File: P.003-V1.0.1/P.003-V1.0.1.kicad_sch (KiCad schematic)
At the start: 0 parts

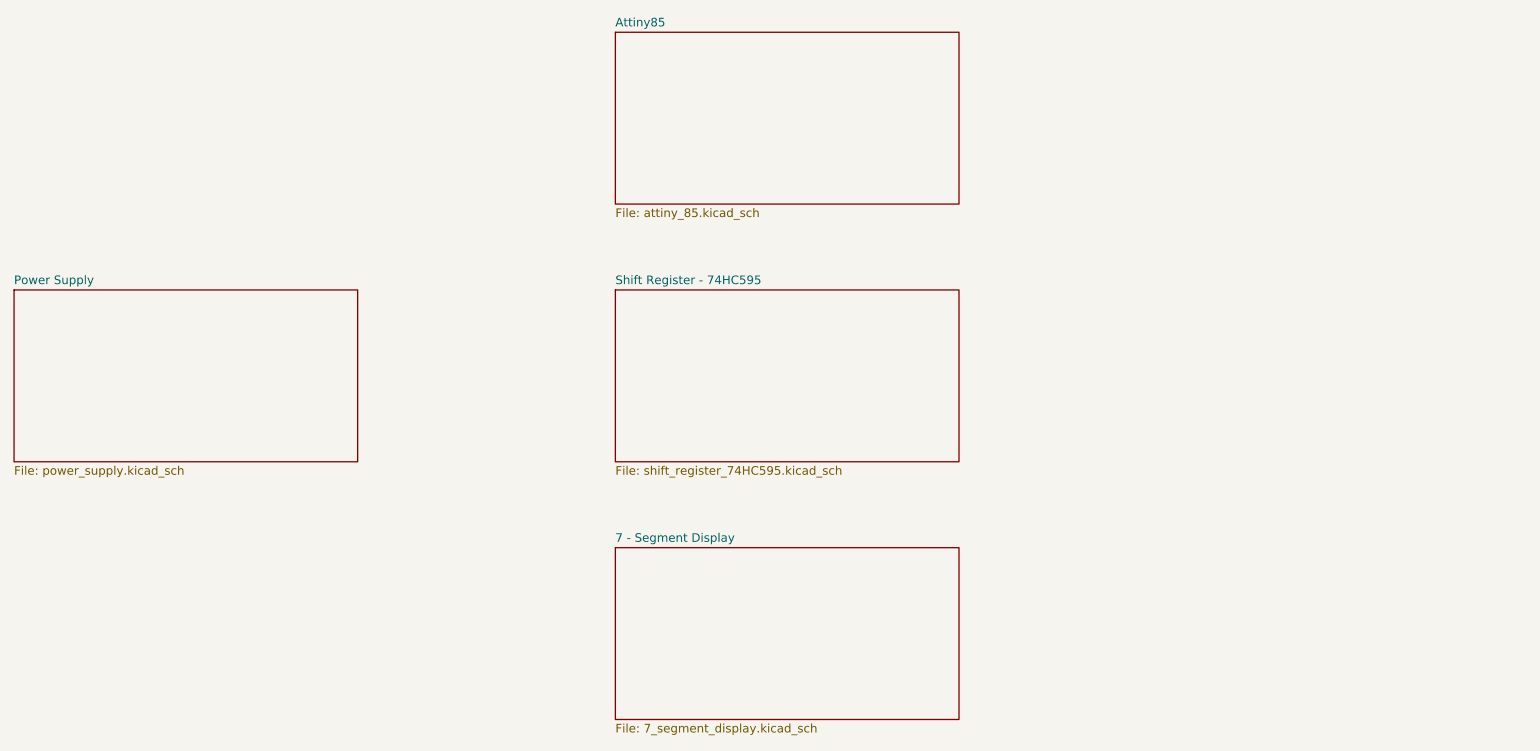
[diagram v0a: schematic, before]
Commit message: add kicad
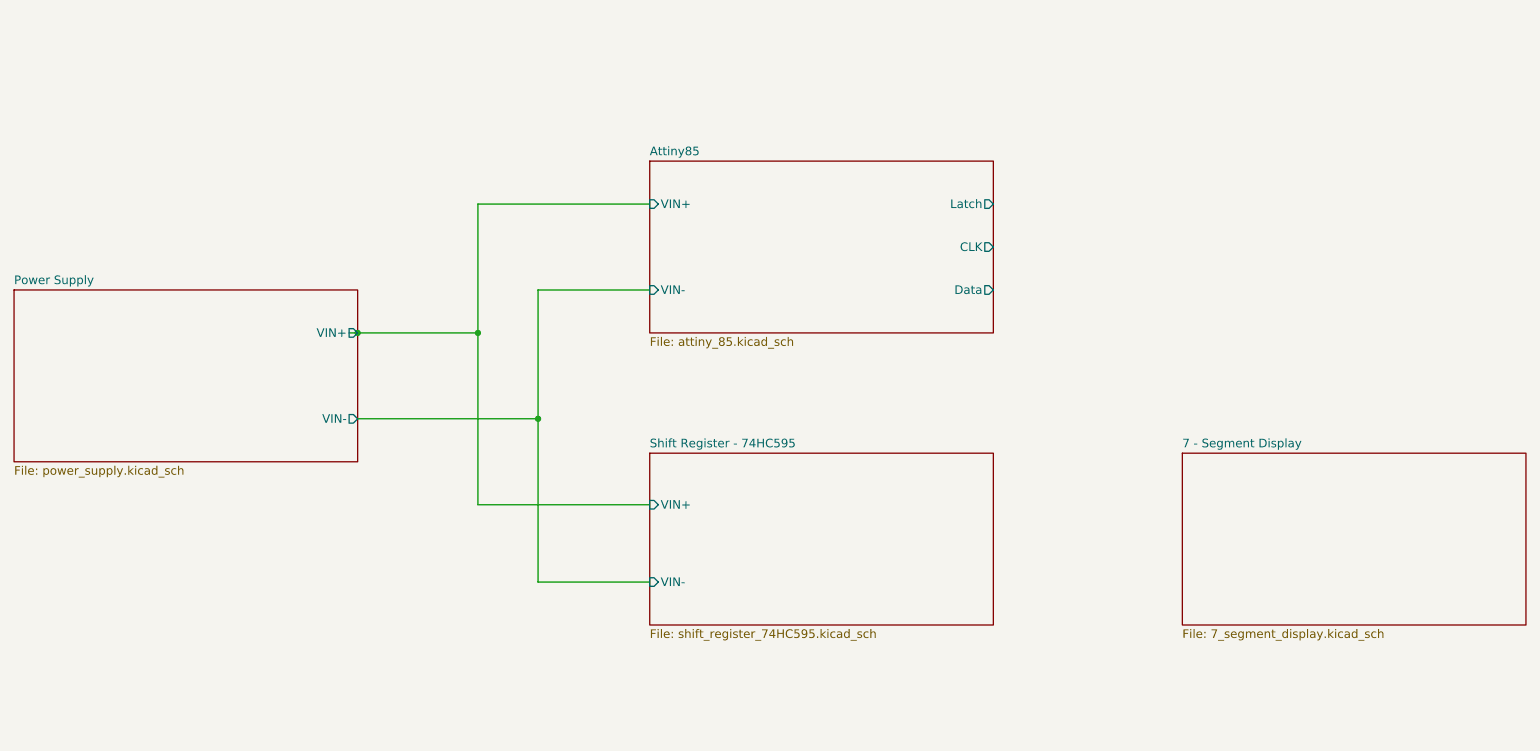
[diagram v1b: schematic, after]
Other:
- sheet Attiny85 ports: added CLK, Data, Latch, VIN+, VIN-; removed none
- sheet Power Supply ports: added VIN+, VIN-; removed none
- sheet Shift Register - 74HC595 ports: added VIN+, VIN-; removed none
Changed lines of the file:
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@@
 	(generator_version "10.0")
 	(paper "A4")
+	(junction
+		(at 88.9 69.85)
+		(diameter 0)
+		(color 0 0 0 0)
+	)
+	(junction
+		(at 106.68 69.85)
+		(diameter 0)
+		(color 0 0 0 0)
+	)
+	(junction
+		(at 115.57 82.55)
+		(diameter 0)
+		(color 0 0 0 0)
+	)
+	(wire
+		(pts
+			(xy 115.57 63.5) (xy 115.57 82.55)
+		)
+		(stroke
+			(width 0)
+			(type default)
+		)
+	)
+	(wire
+		(pts
+			(xy 106.68 95.25) (xy 132.08 95.25)
+		)
+		(stroke
+			(width 0)
+			(type default)
+		)
+	)
+	(wire
+		(pts
+			(xy 88.9 82.55) (xy 115.57 82.55)
+		)
+		(stroke
+			(width 0)
+			(type default)
+		)
+	)
+	(wire
+		(pts
+			(xy 106.68 50.8) (xy 132.08 50.8)
+		)
+		(stroke
+			(width 0)
+			(type default)
+		)
+	)
+	(wire
+		(pts
+			(xy 106.68 69.85) (xy 106.68 95.25)
+		)
+		(stroke
+			(width 0)
+			(type default)
+		)
+	)
+	(wire
+		(pts
+			(xy 115.57 106.68) (xy 115.57 82.55)
+		)
+		(stroke
+			(width 0)
+			(type default)
+		)
+	)
+	(wire
+		(pts
+			(xy 115.57 63.5) (xy 132.08 63.5)
+		)
+		(stroke
+			(width 0)
+			(type default)
+		)
+	)
+	(wire
+		(pts
+			(xy 87.63 69.85) (xy 88.9 69.85)
+		)
+		(stroke
+			(width 0)
+			(type default)
+		)
+	)
+	(wire
+		(pts
+			(xy 132.08 106.68) (xy 115.57 106.68)
+		)
+		(stroke
+			(width 0)
+			(type default)
+		)
+	)
+	(wire
+		(pts
+			(xy 106.68 50.8) (xy 106.68 69.85)
+		)
+		(stroke
+			(width 0)
+			(type default)
+		)
+	)
+	(wire
+		(pts
+			(xy 88.9 69.85) (xy 106.68 69.85)
+		)
+		(stroke
+			(width 0)
+			(type default)
+		)
+	)
 	(sheet
-		(at 127 63.5)
+		(at 132.08 87.63)
 		(size 50.8 25.4)
 		(exclude_from_sim no)
@@
 		)
 		(property "Sheetname" "Shift Register - 74HC595"
-			(at 127 62.7884 0)
+			(at 132.08 86.9184 0)
 			(show_name yes)
 			(do_not_autoplace no)
@@
 		)
 		(property "Sheetfile" "shift_register_74HC595.kicad_sch"
-			(at 127 89.4846 0)
+			(at 132.08 113.6146 0)
 			(show_name yes)
 			(do_not_autoplace no)
@@
 				)
 				(justify left top)
+			)
+		)
+		(pin "VIN+" input
+			(at 132.08 95.25 180)
+			(effects
+				(font
+					(size 1.27 1.27)
+				)
+				(justify left)
+			)
+		)
+		(pin "VIN-" input
+			(at 132.08 106.68 180)
+			(effects
+				(font
+					(size 1.27 1.27)
+				)
+				(justify left)
 			)
 		)
@@
 	)
 	(sheet
-		(at 127 101.6)
+		(at 210.82 87.63)
 		(size 50.8 25.4)
 		(exclude_from_sim no)
@@
 		)
 		(property "Sheetname" "7 - Segment Display"
-			(at 127 100.8884 0)
+			(at 210.82 86.9184 0)
 			(show_name yes)
 			(do_not_autoplace no)
@@
 		)
 		(property "Sheetfile" "7_segment_display.kicad_sch"
-			(at 127 127.5846 0)
+			(at 210.82 113.6146 0)
 			(show_name yes)
 			(do_not_autoplace no)
@@
 			)
 		)
+		(pin "VIN+" output
+			(at 88.9 69.85 0)
+			(effects
+				(font
+					(size 1.27 1.27)
+				)
+				(justify right)
+			)
+		)
+		(pin "VIN-" output
+			(at 88.9 82.55 0)
+			(effects
+				(font
+					(size 1.27 1.27)
+				)
+				(justify right)
+			)
+		)
 		(instances
 			(project "P.003-V1.0.1"
@@
 	)
 	(sheet
-		(at 127 25.4)
+		(at 132.08 44.45)
 		(size 50.8 25.4)
 		(exclude_from_sim no)
@@
 		)
 		(property "Sheetname" "Attiny85"
-			(at 127 24.6884 0)
+			(at 132.08 43.7384 0)
 			(show_name yes)
 			(do_not_autoplace no)
@@
 		)
 		(property "Sheetfile" "attiny_85.kicad_sch"
-			(at 127 51.3846 0)
+			(at 132.08 70.4346 0)
 			(show_name yes)
 			(do_not_autoplace no)
@@
 			)
 		)
+		(pin "CLK" output
+			(at 182.88 57.15 0)
+			(effects
+				(font
+					(size 1.27 1.27)
+				)
+				(justify right)
+			)
+		)
+		(pin "Data" output
+			(at 182.88 63.5 0)
+			(effects
+				(font
+					(size 1.27 1.27)
+				)
+				(justify right)
+			)
+		)
+		(pin "Latch" output
+			(at 182.88 50.8 0)
+			(effects
+				(font
+					(size 1.27 1.27)
+				)
+				(justify right)
+			)
+		)
+		(pin "VIN+" input
+			(at 132.08 50.8 180)
+			(effects
+				(font
+					(size 1.27 1.27)
+				)
+				(justify left)
+			)
+		)
+		(pin "VIN-" input
+			(at 132.08 63.5 180)
+			(effects
+				(font
+					(size 1.27 1.27)
+				)
+				(justify left)
+			)
+		)

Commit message: Schematic wired
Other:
- sheet 7 - Segment Display renamed Display 7 Segment
- sheet Display 7 Segment ports: added Q0, Q1, Q2, Q3, Q4, Q5, Q6, Q7, VIN-; removed none
- sheet Shift Register - 74HC595 ports: added CLK, Data, Latch, Q0, Q1, Q2, Q3, Q4, Q5, Q6, Q7; removed none
- company: (none) -> GSAS - Labs
- title: (none) -> Electronic Dice
